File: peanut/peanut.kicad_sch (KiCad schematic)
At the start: 34 parts, among them J3 USB-C, Q6 NMOS, U4 MS5611-01BA, U5 ESP32-C3FH4, Y1 32.768kHz, Y3 40MHz

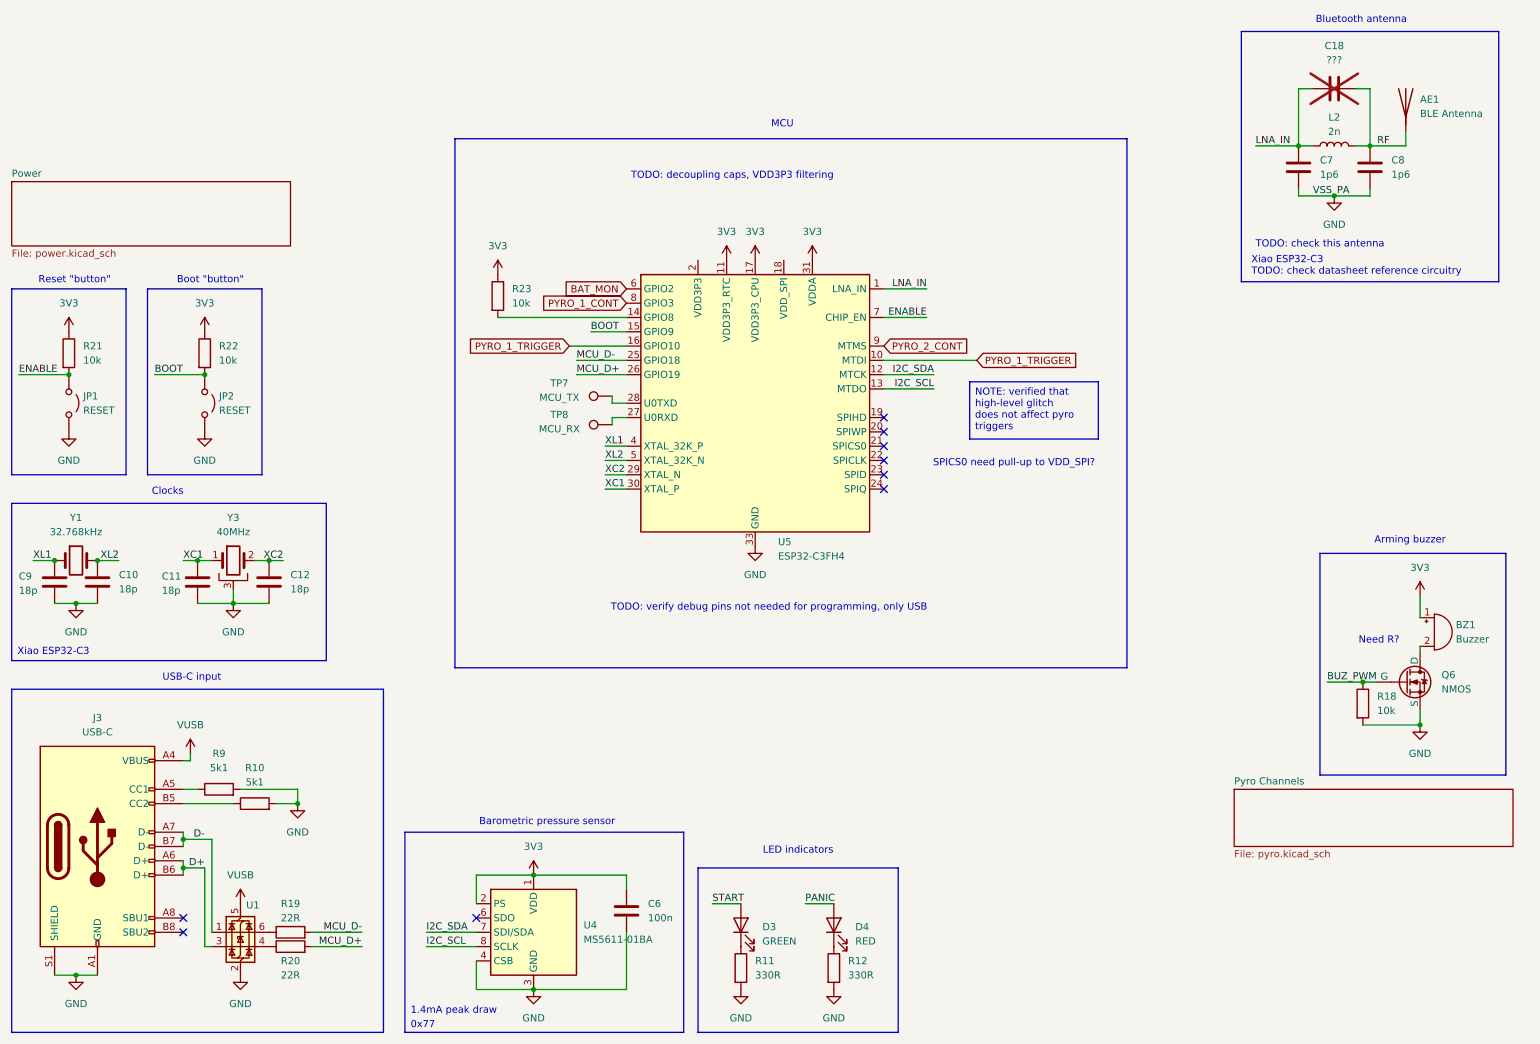
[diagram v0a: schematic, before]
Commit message: Assigned some actual parts and footprints to symbols.
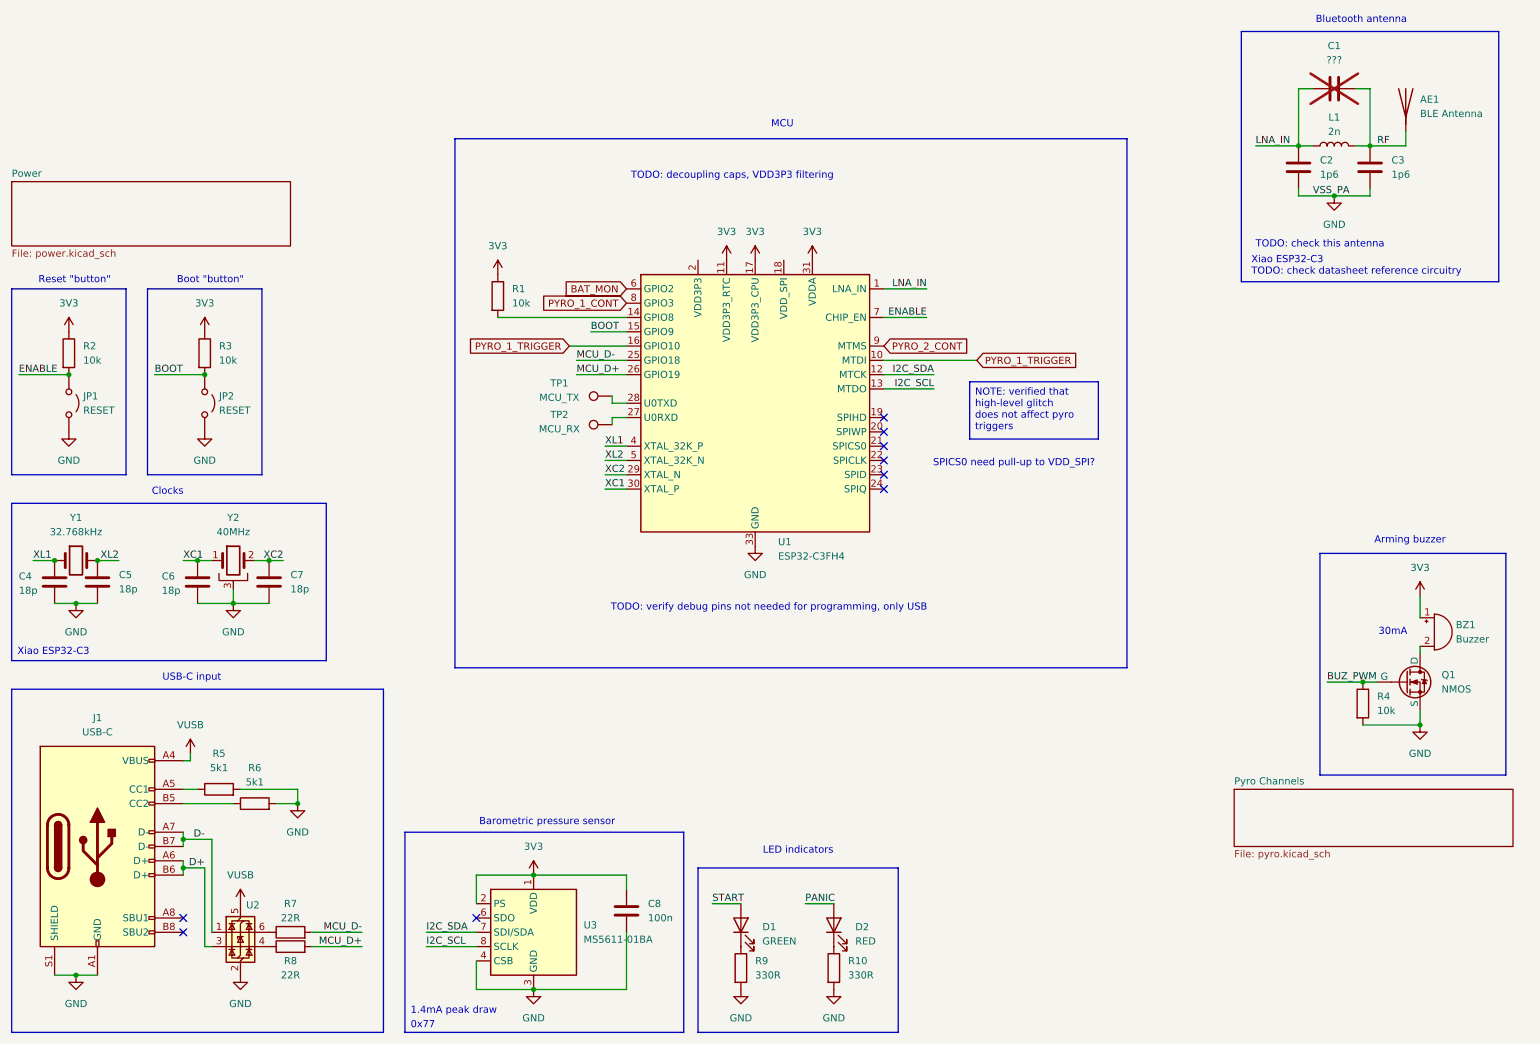
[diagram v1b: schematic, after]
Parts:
- BZ1: MPN (none) -> CMI-0955-03TH
- C1: renamed from C18; footprint (none) -> Capacitor_SMD:C_0402_1005Metric
- C2: renamed from C7; footprint (none) -> Capacitor_SMD:C_0402_1005Metric
- C3: renamed from C8; footprint (none) -> Capacitor_SMD:C_0402_1005Metric
- C4: renamed from C9; footprint (none) -> Capacitor_SMD:C_0402_1005Metric
- C5: renamed from C10; footprint (none) -> Capacitor_SMD:C_0402_1005Metric
- C6: renamed from C11; footprint (none) -> Capacitor_SMD:C_0402_1005Metric
- C7: renamed from C12; footprint (none) -> Capacitor_SMD:C_0402_1005Metric
- C8: renamed from C6; footprint (none) -> Capacitor_SMD:C_0402_1005Metric
- D1: renamed from D3; footprint (none) -> LED_SMD:LED_0402_1005Metric
- D2: renamed from D4; footprint (none) -> LED_SMD:LED_0402_1005Metric
- J1: renamed from J3; footprint (none) -> Connector_USB:USB_C_Receptacle_GCT_USB4105-xx-A_16P_TopMnt_Horizontal
- JP1, JP2: footprint (none) -> Capacitor_SMD:C_0805_2012Metric
- R1: renamed from R23; footprint (none) -> Resistor_SMD:R_0402_1005Metric
- R10: renamed from R12; footprint (none) -> Resistor_SMD:R_0402_1005Metric
- R2: renamed from R21; footprint (none) -> Resistor_SMD:R_0402_1005Metric
- R3: renamed from R22; footprint (none) -> Resistor_SMD:R_0402_1005Metric
- R4: renamed from R18; footprint (none) -> Resistor_SMD:R_0402_1005Metric
- R5: renamed from R9; footprint (none) -> Resistor_SMD:R_0402_1005Metric
- R6: renamed from R10; footprint (none) -> Resistor_SMD:R_0402_1005Metric
- R7: renamed from R19; footprint (none) -> Resistor_SMD:R_0402_1005Metric
- R8: renamed from R20; footprint (none) -> Resistor_SMD:R_0402_1005Metric
- R9: renamed from R11; footprint (none) -> Resistor_SMD:R_0402_1005Metric
- TP1: renamed from TP7; footprint (none) -> TestPoint:TestPoint_Pad_D1.0mm
- TP2: renamed from TP8; footprint (none) -> TestPoint:TestPoint_Pad_D1.0mm
- U1: renamed from U5; footprint Package_DFN_QFN:QFN-32-1EP_5x5mm_P0.5mm_EP3.7x3.7mm -> Package_TO_SOT_SMD:SOT-23-6
- U2: renamed from U1; footprint Package_TO_SOT_SMD:SOT-23-6 -> Package_TO_SOT_SMD:SOT-583-8
- U3: renamed from U4; footprint Package_LGA:LGA-8_3x5mm_P1.25mm -> Package_TO_SOT_SMD:TSOT-23-5
- Y1: footprint (none) -> Crystal:Crystal_SMD_MicroCrystal_CM9V-T1A-2Pin_1.6x1.0mm; MPN (none) -> 9HT12-32.768KDZF-T
- renumbered L2 to L1, Q6 to Q1, Y3 to Y2
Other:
- note added: "30mA"
- note removed: "Need R?"

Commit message: Footprint assignments for dual-channel NMOS; picked some more parts
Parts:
- D1: footprint LED_SMD:LED_0402_1005Metric -> LED_SMD:LED_0805_2012Metric; MPN (none) -> HSMG-C170
- D2: footprint LED_SMD:LED_0402_1005Metric -> LED_SMD:LED_0805_2012Metric; MPN (none) -> HSMC-C170-T0000
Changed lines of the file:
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@@
 			)
 		)
-		(property "Footprint" "LED_SMD:LED_0402_1005Metric"
+		(property "Footprint" "LED_SMD:LED_0805_2012Metric"
 			(at 161.29 176.53 0)
 			(effects
@@
 			)
 		)
-		(property "MPN" ""
+		(property "MPN" " HSMC-C170-T0000"
 			(at 161.29 176.53 90)
 			(effects
@@
 			)
 		)
-		(property "Footprint" "LED_SMD:LED_0402_1005Metric"
+		(property "Footprint" "LED_SMD:LED_0805_2012Metric"
 			(at 144.78 176.53 0)
 			(effects
@@
 			)
 		)
-		(property "MPN" ""
+		(property "MPN" " HSMG-C170"
 			(at 144.78 176.53 90)
 			(effects

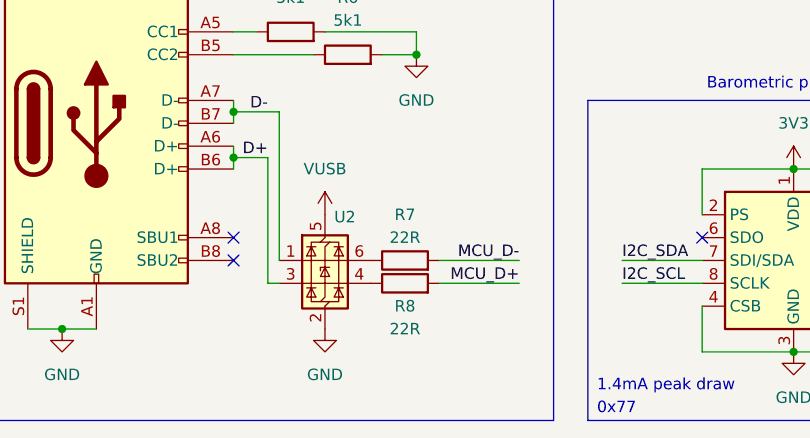
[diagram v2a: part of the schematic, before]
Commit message: More component MPNs
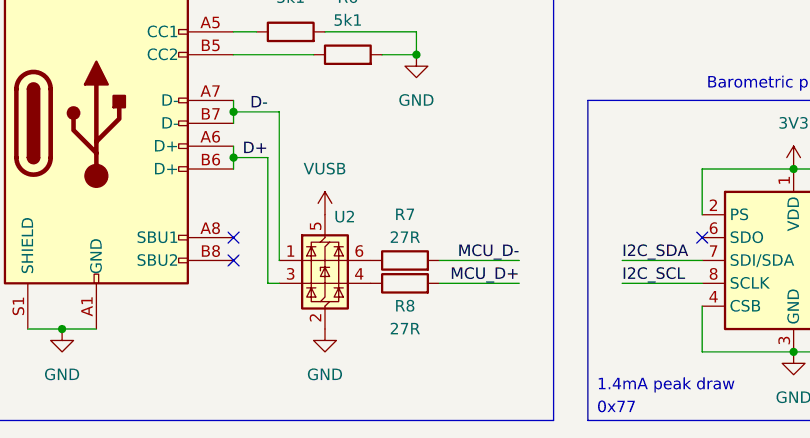
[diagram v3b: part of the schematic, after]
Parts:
- C8: MPN (none) -> GRM155R61A104KA01J
- D1: MPN HSMG-C170 -> HSMG-C170
- D2: MPN HSMC-C170-T0000 -> HSMC-C170-T0000
- J1: MPN (none) -> USB4215-03-A
- Q1: footprint (none) -> Package_TO_SOT_SMD:SOT-23-3; MPN (none) -> BSS138IXTSA1
- R1, R2, R3, R4: MPN (none) -> SFR01MZPJ103
- R10, R9: MPN (none) -> 560112110231
- R5, R6: MPN (none) -> MCS04020C5101FE000
- R7, R8: value 22R -> 27R; MPN (none) -> ERA-2AKD270X
- U1: footprint Package_TO_SOT_SMD:SOT-23-6 -> Package_DFN_QFN:QFN-32-1EP_5x5mm_P0.5mm_EP3.7x3.7mm; MPN (none) -> ESP32-C3FH4
- U2: footprint Package_TO_SOT_SMD:SOT-583-8 -> Package_TO_SOT_SMD:SOT-23-6; MPN (none) -> USBLC6-2SC6
- U3: footprint Package_TO_SOT_SMD:TSOT-23-5 -> Package_LGA:LGA-8_3x5mm_P1.25mm; MPN (none) -> MS561101BA03-50
- Y1: MPN 9HT12-32.768KDZF-T -> 9HT12-32.768KDZF-T
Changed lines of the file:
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@@
 			)
 		)
-		(property "MPN" ""
+		(property "MPN" "560112110231"
 			(at 161.29 184.15 0)
 			(effects
@@
 			)
 		)
-		(property "Footprint" ""
+		(property "Footprint" "Package_TO_SOT_SMD:SOT-23-3"
 			(at 267.97 130.81 0)
 			(effects
@@
 			)
 		)
-		(property "MPN" ""
+		(property "MPN" "BSS138IXTSA1"
 			(at 262.89 133.35 0)
 			(effects
@@
 			)
 		)
-		(property "MPN" " HSMC-C170-T0000"
+		(property "MPN" "HSMC-C170-T0000"
 			(at 161.29 176.53 90)
 			(effects
@@
 			)
 		)
-		(property "MPN" " 9HT12-32.768KDZF-T "
+		(property "MPN" "9HT12-32.768KDZF-T "
 			(at 26.67 111.76 0)
 			(effects
@@
 			)
 		)
-		(property "MPN" ""
+		(property "MPN" "USB4215-03-A"
 			(at 30.48 162.56 0)
 			(effects
@@
 			)
 		)
-		(property "MPN" ""
+		(property "MPN" "GRM155R61A104KA01J"
 			(at 124.46 173.99 0)
 			(effects
@@
 			)
 		)
-		(property "MPN" " HSMG-C170"
+		(property "MPN" "HSMG-C170"
 			(at 144.78 176.53 90)
 			(effects
@@
 			)
 		)
-		(property "MPN" ""
+		(property "MPN" "SFR01MZPJ103"
 			(at 25.4 74.93 0)
 			(effects
@@
 			)
 		)
-		(property "MPN" ""
+		(property "MPN" "SFR01MZPJ103"
 			(at 101.6 64.77 0)
 			(effects
@@
 			)
 		)
-		(property "Value" "22R"
+		(property "Value" "27R"
 			(at 64.77 185.42 90)
 			(effects
@@
 			)
 		)
-		(property "MPN" ""
+		(property "MPN" "ERA-2AKD270X"
 			(at 64.77 180.34 90)
 			(effects
@@
 			)
 		)
-		(property "MPN" ""
+		(property "MPN" "MCS04020C5101FE000"
 			(at 58.42 154.94 90)
 			(effects
@@
 			)
 		)
-		(property "MPN" ""
+		(property "MPN" "SFR01MZPJ103"
 			(at 49.53 74.93 0)
 			(effects
@@
 			)
 		)
-		(property "MPN" ""
+		(property "MPN" "560112110231"
 			(at 144.78 184.15 0)
 			(effects
@@
 			)
 		)
-		(property "Value" "22R"
+		(property "Value" "27R"
 			(at 64.77 175.26 90)
 			(effects
@@
 			)
 		)
-		(property "MPN" ""
+		(property "MPN" "ERA-2AKD270X"
 			(at 64.77 177.8 90)
 			(effects
@@
 			)
 		)
-		(property "Footprint" "Package_TO_SOT_SMD:TSOT-23-5"
+		(property "Footprint" "Package_LGA:LGA-8_3x5mm_P1.25mm"
 			(at 107.95 177.8 0)
 			(effects
@@
 			)
 		)
-		(property "MPN" ""
+		(property "MPN" "MS561101BA03-50"
 			(at 107.95 177.8 0)
 			(effects
@@
 			)
 		)
-		(property "Footprint" "Package_TO_SOT_SMD:SOT-23-6"
+		(property "Footprint" "Package_DFN_QFN:QFN-32-1EP_5x5mm_P0.5mm_EP3.7x3.7mm"
 			(at 147.828 83.82 0)
 			(effects
@@
 			)
 		)
-		(property "MPN" ""
+		(property "MPN" "ESP32-C3FH4 "
 			(at 147.32 83.82 0)
 			(effects
@@
 			)
 		)
-		(property "Footprint" "Package_TO_SOT_SMD:SOT-583-8"
+		(property "Footprint" "Package_TO_SOT_SMD:SOT-23-6"
 			(at 57.15 184.15 0)
 			(effects
@@
 			)
 		)
-		(property "MPN" ""
+		(property "MPN" "USBLC6-2SC6"
 			(at 55.88 177.8 0)
 			(effects
@@
 			)
 		)
-		(property "MPN" ""
+		(property "MPN" "MCS04020C5101FE000"
 			(at 52.07 152.4 90)
 			(effects
@@
 			)
 		)
-		(property "MPN" ""
+		(property "MPN" "SFR01MZPJ103"
 			(at 255.27 137.16 0)
 			(effects
